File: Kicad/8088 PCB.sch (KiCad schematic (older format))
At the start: 74 parts, among them J1 Bus_ISA_8bit, J2 Mini-DIN-6, J3 SPK, SW1 RESET, U1 8088, U10 8237, U11 74LS573, U12 74LS139, U13 AS6C4008, U14 AS6C1008, U15 27C512, U16 74LS138, U17 8284, U18 74LS74, U19 W83C42P, U2 74LS573, U20 74LS07, U21 74LS04, U22 8284, U23 74LS245, U24 74LS573, U25 74LS126, U26 74LS125, U3 74LS573, U4 74LS245, U5 8254, U6 8259, U7 74LS670, U8 74LS257, U9 27C512, Y1 14.31818, Y2 CRYSTAL

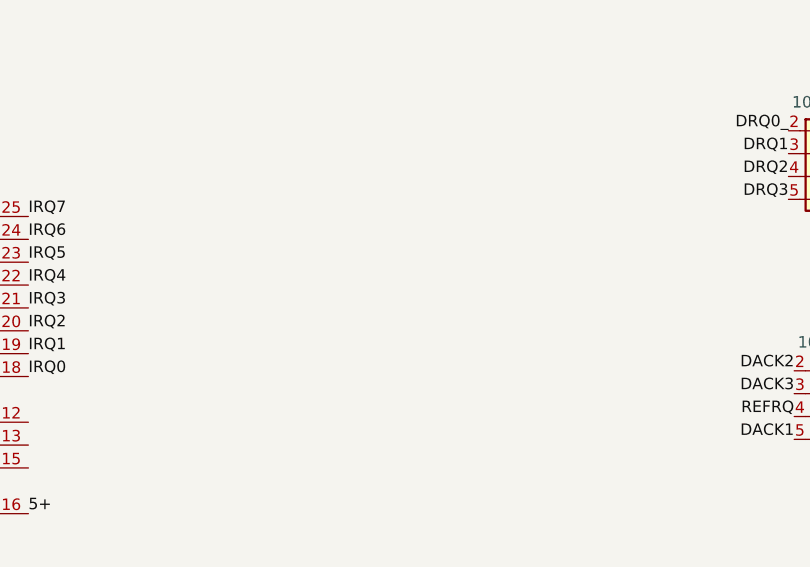
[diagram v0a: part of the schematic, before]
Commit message: Added CH376 conn
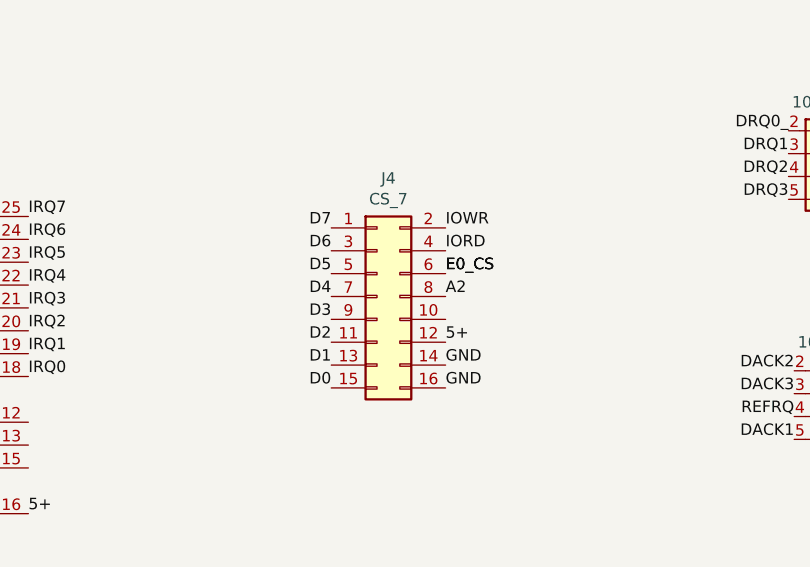
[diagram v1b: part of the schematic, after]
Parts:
- added J4: CS_7, Connector_PinHeader_2.54mm:PinHeader_2x08_P2.54mm_Vertical, symbol Connector_Generic:Conn_02x08_Odd_Even
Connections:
- net 5+: now also J4.12 (Pin_12)
- net A2: now also J4.8 (Pin_8)
- net D0: now also J4.15 (Pin_15)
- net D1: now also J4.13 (Pin_13)
- net D2: now also J4.11 (Pin_11)
- net D3: now also J4.9 (Pin_9)
- net D4: now also J4.7 (Pin_7)
- net D5: now also J4.5 (Pin_5)
- net D6: now also J4.3 (Pin_3)
- net D7: now also J4.1 (Pin_1)
- net E0_CS: now also J4.6 (Pin_6)
- net GND: now also J4.14 (Pin_14), J4.16 (Pin_16)
- net IORD: now also J4.4 (Pin_4)
- net IOWR: now also J4.2 (Pin_2)
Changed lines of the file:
@@
 Text Label 12500 5575 2    50   ~ 0
 CH_CK_
+$Comp
+L Connector_Generic:Conn_02x08_Odd_Even J4
+U 1 1 6634FD55
+P 12825 1800
+F 0 "J4" H 12875 2317 50  0000 C CNN
+F 1 "CS_7" H 12875 2226 50  0000 C CNN
+F 2 "Connector_PinHeader_2.54mm:PinHeader_2x08_P2.54mm_Vertical" H 12825 1800 50  0001 C CNN
+F 3 "~" H 12825 1800 50  0001 C CNN
+	1    12825 1800
+	1    0    0    -1
+$EndComp
+Text Label 12625 1500 2    50   ~ 0
+D7
+Text Label 12625 1600 2    50   ~ 0
+D6
+Text Label 12625 1700 2    50   ~ 0
+D5
+Text Label 12625 1800 2    50   ~ 0
+D4
+Text Label 12625 1900 2    50   ~ 0
+D3
+Text Label 12625 2000 2    50   ~ 0
+D2
+Text Label 12625 2100 2    50   ~ 0
+D1
+Text Label 12625 2200 2    50   ~ 0
+D0
+Text Label 13125 1500 0    50   ~ 0
+IOWR
+Text Label 13125 1600 0    50   ~ 0
+IORD
+Text Label 13125 1700 0    50   ~ 0
+E0_CS
+Text Label 13125 1700 0    50   ~ 0
+E0_CS
+Text Label 13125 1800 0    50   ~ 0
+A2
+Text Label 13125 2000 0    50   ~ 0
+5+
+Text Label 13125 2100 0    50   ~ 0
+GND
+Text Label 13125 2200 0    50   ~ 0
+GND
 $EndSCHEMATC

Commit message: update for production
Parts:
- added R10, R8: 10K OHM, Resistor_THT:R_Array_SIP5, symbol Device:R_Network04
- added unit 6 of U21
- J4: value CS_7 -> CS7
- R12: footprint Resistor_THT:R_Array_SIP4 -> Resistor_THT:R_Array_SIP7; symbol Device:R_Network03 -> Device:R_Network06
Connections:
- net 00_CS: now also R8.5 (R4)
- net 20_CS: now also R8.4 (R3)
- net 40_CS: now also R8.3 (R2)
- net 5+: now also R10.1 (common), R8.1 (common)
- net 60_CS: now also R10.2 (R1)
- net 61_CS: now also R10.3 (R2)
- net 760_WR: now also R12.7 (R6)
- net 80_CS: now also R10.4 (R3)
- net AEN: now also R12.6 (R5)
- net CH_CK_: now also R12.5 (R4); no longer R12.4 (R3)
- net E0_CS: now also R10.5 (R4)
- net EOP: now also R12.4 (R3)
- net HOLDA: no longer U9.22 (~OE)
- net IOM: now also U21.13
- net NMI: now also R14.4 (R3)
- net RDY1: now also R8.2 (R1)
- new net IOM_: U21.12, U9.22 (~OE)
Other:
- moved on the sheet: U21G
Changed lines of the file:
@@
 L 74xx:74LS04 U21
 U 7 1 662A70C3
-P 14275 8200
-F 0 "U21" V 13908 8200 50  0000 C CNN
-F 1 "74LS04" V 13999 8200 50  0000 C CNN
-F 2 "Package_DIP:DIP-14_W7.62mm" H 14275 8200 50  0001 C CNN
-F 3 "http://www.ti.com/lit/gpn/sn74LS04" H 14275 8200 50  0001 C CNN
-	7    14275 8200
+P 14250 8900
+F 0 "U21" V 13883 8900 50  0000 C CNN
+F 1 "74LS04" V 13974 8900 50  0000 C CNN
+F 2 "Package_DIP:DIP-14_W7.62mm" H 14250 8900 50  0001 C CNN
+F 3 "http://www.ti.com/lit/gpn/sn74LS04" H 14250 8900 50  0001 C CNN
+	7    14250 8900
 	0    1    1    0
 $EndComp
 Text Label 13950 6150 2    50   ~ 0
 KBD_CLK
-Text Label 14775 8200 0    50   ~ 0
-5+
-Text Label 13775 8200 2    50   ~ 0
+Text Label 14750 8900 0    50   ~ 0
+5+
+Text Label 13750 8900 2    50   ~ 0
 GND
 Text Label 14475 5825 0    50   ~ 0
@@
 Text Label 11100 6000 2    50   ~ 0
 IOWR
-Text Label 12900 5375 0    50   ~ 0
+Text Label 12900 5275 0    50   ~ 0
 5+
 Text Label 11700 6000 0    50   ~ 0
@@
 Text Label 7225 6850 2    50   ~ 0
 CS_61_RD
-Text Label 12500 5375 2    50   ~ 0
+Text Label 12500 5275 2    50   ~ 0
 CS_61_WR
 Text Label 11825 7100 0    50   ~ 0
@@
 GND
 $Comp
-L Device:R_Network03 R12
+L Device:R_Network06 R12
 U 1 1 66279E14
-P 12700 5475
-F 0 "R12" V 12425 5475 50  0000 C CNN
-F 1 "10K OHM" V 12500 5475 50  0000 C CNN
-F 2 "Resistor_THT:R_Array_SIP4" V 12630 5475 50  0001 C CNN
-F 3 "~" H 12700 5475 50  0001 C CNN
-	1    12700 5475
-	0    1    1    0
-$EndComp
-Text Label 12500 5475 2    50   ~ 0
+P 12700 5575
+F 0 "R12" V 12425 5575 50  0000 C CNN
+F 1 "10K OHM" V 12300 5550 50  0000 C CNN
+F 2 "Resistor_THT:R_Array_SIP7" V 12630 5575 50  0001 C CNN
+F 3 "~" H 12700 5575 50  0001 C CNN
+	1    12700 5575
+	0    1    1    0
+$EndComp
+Text Label 12500 5375 2    50   ~ 0
 CS_61_RD
 $Comp
@@
 Text Label 975  5525 2    50   ~ 0
 PU1
-Text Label 6275 2800 2    50   ~ 0
-HOLDA
 Text Label 6275 1900 2    50   ~ 0
 A9
@@
 P 12825 1800
 F 0 "J4" H 12875 2317 50  0000 C CNN
-F 1 "CS_7" H 12875 2226 50  0000 C CNN
+F 1 "CS7" H 12875 2226 50  0000 C CNN
 F 2 "Connector_PinHeader_2.54mm:PinHeader_2x08_P2.54mm_Vertical" H 12825 1800 50  0001 C CNN
 F 3 "~" H 12825 1800 50  0001 C CNN
@@
 Text Label 13125 2200 0    50   ~ 0
 GND
+$Comp
+L 74xx:74LS04 U21
+U 6 1 6634F801
+P 14275 8200
+F 0 "U21" H 14275 8517 50  0000 C CNN
+F 1 "74LS04" H 14275 8426 50  0000 C CNN
+F 2 "Package_DIP:DIP-14_W7.62mm" H 14275 8200 50  0001 C CNN
+F 3 "http://www.ti.com/lit/gpn/sn74LS04" H 14275 8200 50  0001 C CNN
+	6    14275 8200
+	1    0    0    -1
+$EndComp
+Text Label 13975 8200 2    50   ~ 0
+IOM
+Text Label 14575 8200 0    50   ~ 0
+IOM_
+Text Label 6275 2800 2    50   ~ 0
+IOM_
+$Comp
+L Device:R_Network04 R8
+U 1 1 66350675
+P 6600 3825
+F 0 "R8" V 6325 3825 50  0000 C CNN
+F 1 "10K OHM" V 6400 3825 50  0000 C CNN
+F 2 "Resistor_THT:R_Array_SIP5" V 6530 3825 50  0001 C CNN
+F 3 "~" H 6600 3825 50  0001 C CNN
+	1    6600 3825
+	0    1    1    0
+$EndComp
+Text Label 6800 3625 0    50   ~ 0
+5+
+Text Label 7425 4250 2    50   ~ 0
+E0_CS
+Text Label 7425 4150 2    50   ~ 0
+80_CS
+Text Label 7425 4050 2    50   ~ 0
+61_CS
+Text Label 6400 3725 2    50   ~ 0
+40_CS
+Text Label 6400 3825 2    50   ~ 0
+20_CS
+Text Label 6400 3925 2    50   ~ 0
+00_CS
+Text Label 7425 3950 2    50   ~ 0
+60_CS
+$Comp
+L Device:R_Network04 R10
+U 1 1 66359A39
+P 7625 4150
+F 0 "R10" V 7350 4150 50  0000 C CNN
+F 1 "10K OHM" V 7425 4150 50  0000 C CNN
+F 2 "Resistor_THT:R_Array_SIP5" V 7555 4150 50  0001 C CNN
+F 3 "~" H 7625 4150 50  0001 C CNN
+	1    7625 4150
+	0    1    1    0
+$EndComp
+Text Label 7825 3950 0    50   ~ 0
+5+
+Text Label 3000 5350 2    50   ~ 0
+NMI
+Text Label 12500 5475 2    50   ~ 0
+EOP
+Text Label 12500 5675 2    50   ~ 0
+AEN
+Text Label 6400 3625 2    50   ~ 0
+RDY1
+Text Label 12500 5775 2    50   ~ 0
+760_WR
 $EndSCHEMATC

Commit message: 17 May 24 build
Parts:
- added R15: 10K OHM, Resistor_THT:R_Axial_DIN0207_L6.3mm_D2.5mm_P10.16mm_Horizontal, symbol Device:R
- R12: footprint Resistor_THT:R_Array_SIP7 -> Resistor_THT:R_Array_SIP6; symbol Device:R_Network06 -> Device:R_Network05
- R17: footprint Resistor_THT:R_Array_SIP5 -> Resistor_THT:R_Array_SIP6; symbol Device:R_Network04 -> Device:R_Network05
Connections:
- net 5+: now also U10.5 (PIN5), R15.1
- net 760_WR: now also R12.6 (R5); no longer R12.7 (R6)
- net AEN: now also R17.6 (R5); no longer R12.6 (R5)
- net DEN: now also R15.2; no longer R14.3 (R2)
- net NMI: now also R14.3 (R2); no longer R14.4 (R3)
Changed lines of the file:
@@
 GND
 $Comp
-L Device:R_Network06 R12
+L Device:R_Network05 R12
 U 1 1 66279E14
-P 12700 5575
-F 0 "R12" V 12425 5575 50  0000 C CNN
-F 1 "10K OHM" V 12300 5550 50  0000 C CNN
-F 2 "Resistor_THT:R_Array_SIP7" V 12630 5575 50  0001 C CNN
-F 3 "~" H 12700 5575 50  0001 C CNN
-	1    12700 5575
+P 12700 5475
+F 0 "R12" V 12425 5475 50  0000 C CNN
+F 1 "10K OHM" V 12300 5450 50  0000 C CNN
+F 2 "Resistor_THT:R_Array_SIP6" V 12630 5475 50  0001 C CNN
+F 3 "~" H 12700 5475 50  0001 C CNN
+	1    12700 5475
 	0    1    1    0
 $EndComp
@@
 DACK3
 $Comp
-L Device:R_Network04 R17
+L Device:R_Network05 R17
 U 1 1 662C6187
 P 14825 1275
 F 0 "R17" V 14425 1250 50  0000 C CNN
 F 1 "10K OHM" V 14500 1250 50  0000 C CNN
-F 2 "Resistor_THT:R_Array_SIP5" V 14755 1275 50  0001 C CNN
+F 2 "Resistor_THT:R_Array_SIP6" V 14755 1275 50  0001 C CNN
 F 3 "~" H 14825 1275 50  0001 C CNN
 	1    14825 1275
@@
 Text Label 3000 5150 2    50   ~ 0
 HOLD
-Text Label 3000 5250 2    50   ~ 0
+Text Label 3450 6725 2    50   ~ 0
 DEN
 Text Label 975  5525 2    50   ~ 0
@@
 Text Label 7825 3950 0    50   ~ 0
 5+
-Text Label 3000 5350 2    50   ~ 0
+Text Label 3000 5250 2    50   ~ 0
 NMI
 Text Label 12500 5475 2    50   ~ 0
 EOP
-Text Label 12500 5675 2    50   ~ 0
+Text Label 14625 1475 2    50   ~ 0
 AEN
 Text Label 6400 3625 2    50   ~ 0
 RDY1
-Text Label 12500 5775 2    50   ~ 0
+Text Label 12500 5675 2    50   ~ 0
 760_WR
+Text Label 16875 850  2    50   ~ 0
+5+
+$Comp
+L Device:R R15
+U 1 1 664983E2
+P 3600 6725
+F 0 "R15" V 3393 6725 50  0000 C CNN
+F 1 "10K OHM" V 3484 6725 50  0000 C CNN
+F 2 "Resistor_THT:R_Axial_DIN0207_L6.3mm_D2.5mm_P10.16mm_Horizontal" V 3530 6725 50  0001 C CNN
+F 3 "~" H 3600 6725 50  0001 C CNN
+	1    3600 6725
+	0    1    1    0
+$EndComp
+Text Label 3750 6725 0    50   ~ 0
+5+
 $EndSCHEMATC
